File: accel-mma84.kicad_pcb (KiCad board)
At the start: 2 copper layers, 27.3 x 27.9 mm, 10 parts, among them IC1 AT24CS01-STUM, J2 CONN_01X10, J3 CONN_01X02, U1 MMA8452Q

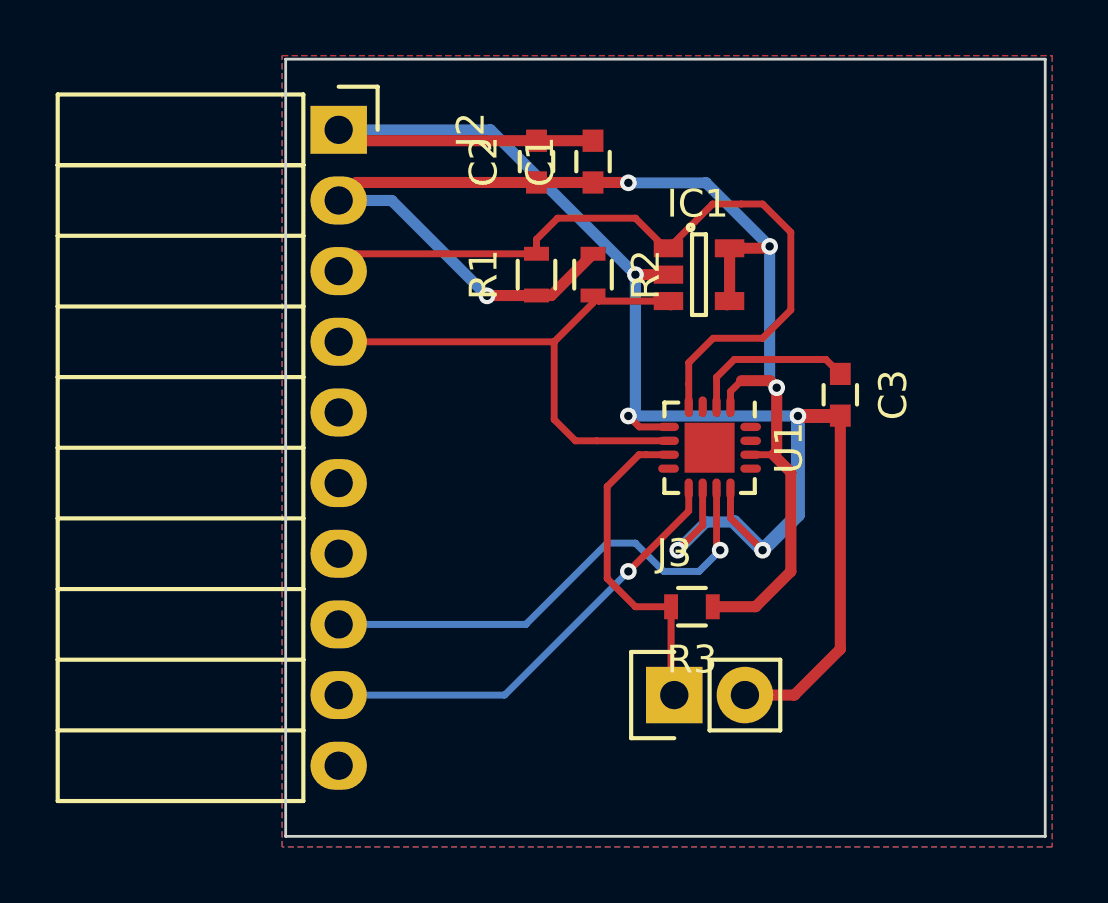
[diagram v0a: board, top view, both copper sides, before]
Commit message: Reduces via count.
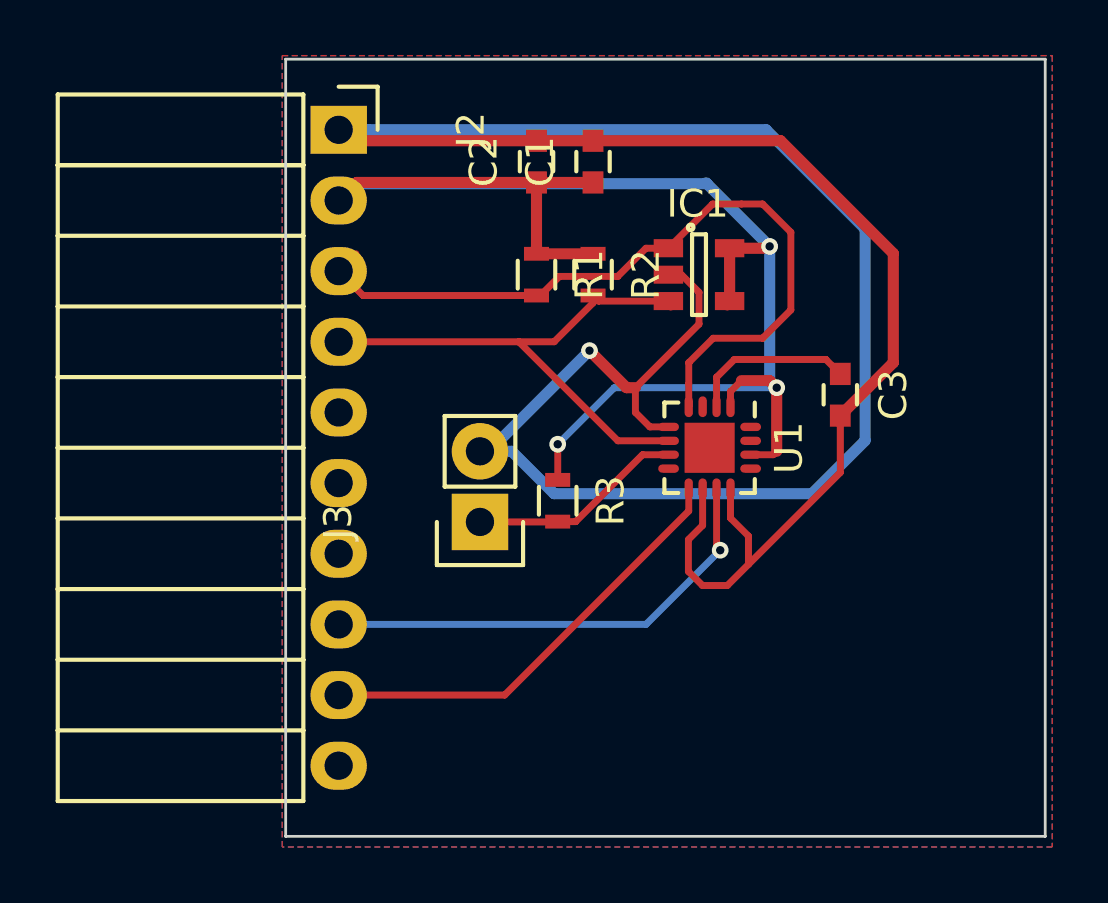
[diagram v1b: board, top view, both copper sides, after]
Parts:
- moved J3 9.35 mm to (129.5, 107.4), turned to 90 degrees
- moved R3 6.15 mm to (132.3, 106.7), turned to 270 degrees
- turned R1 to 270 degrees
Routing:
- net GND: track 68.2 -> 104.6 mm, vias 5 -> 1
- net VCC: track 50.1 -> 55.1 mm, vias 4 -> 3
- net Net-(J3-Pad1): track 11.9 -> 7.78 mm
- net INT1: track 17.9 -> 17.1 mm
- net SCL: track 27.7 -> 28.2 mm
- net INT2: vias 1 -> 0

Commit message: Reorganizes component layout.
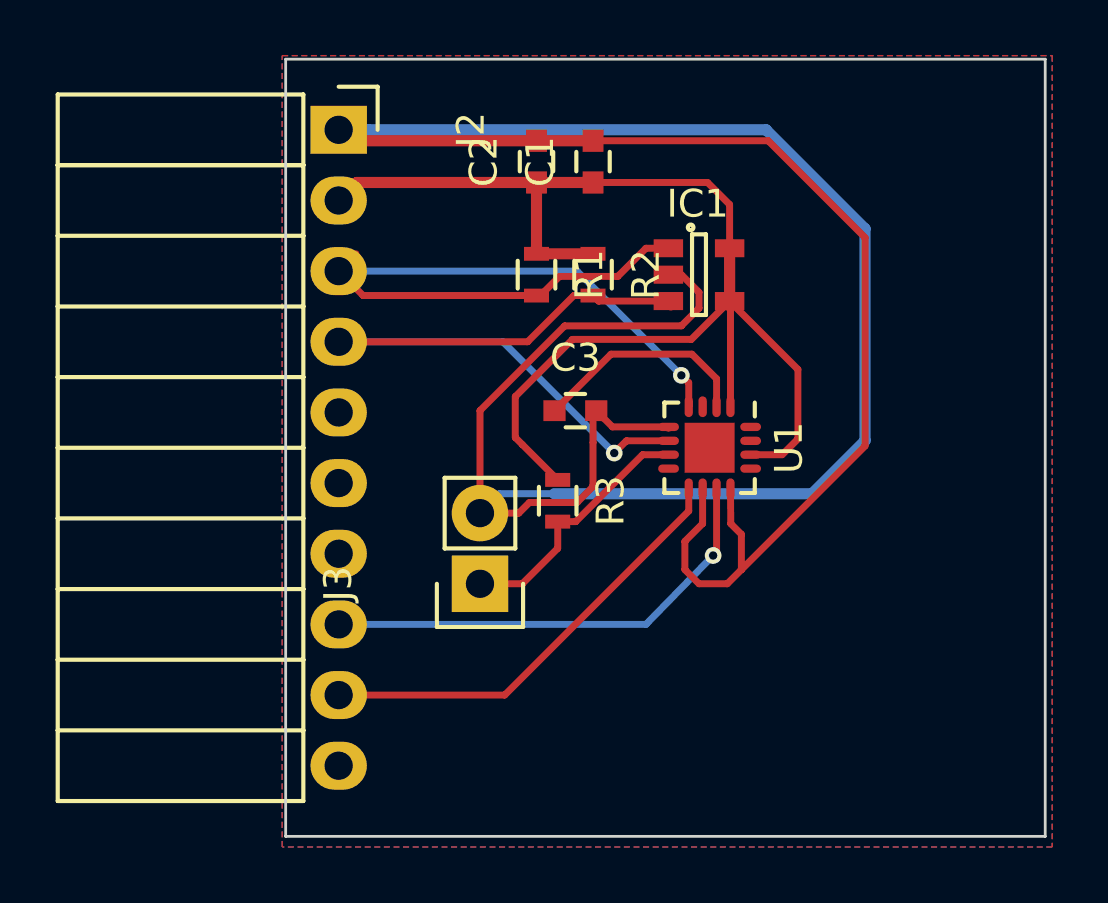
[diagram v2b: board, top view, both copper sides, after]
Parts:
- moved C3 9.54 mm to (133.0, 103.4), turned to 0 degrees
- moved J3 2.22 mm to (129.5, 109.7)
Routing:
- net GND: track 104.6 -> 112.8 mm, vias 1 -> 0
- net SDA: track 20.1 -> 27.3 mm, vias 0 -> 1
- net VCC: track 55.1 -> 48.1 mm, vias 3 -> 0
- net Net-(C3-Pad1): track 5.99 -> 8.04 mm
- net Net-(J3-Pad1): track 7.78 -> 9.28 mm
- net SCL: track 28.2 -> 29.0 mm, vias 0 -> 1
